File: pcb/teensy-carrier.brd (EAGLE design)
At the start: 63.2 x 41.9 mm, 13 parts

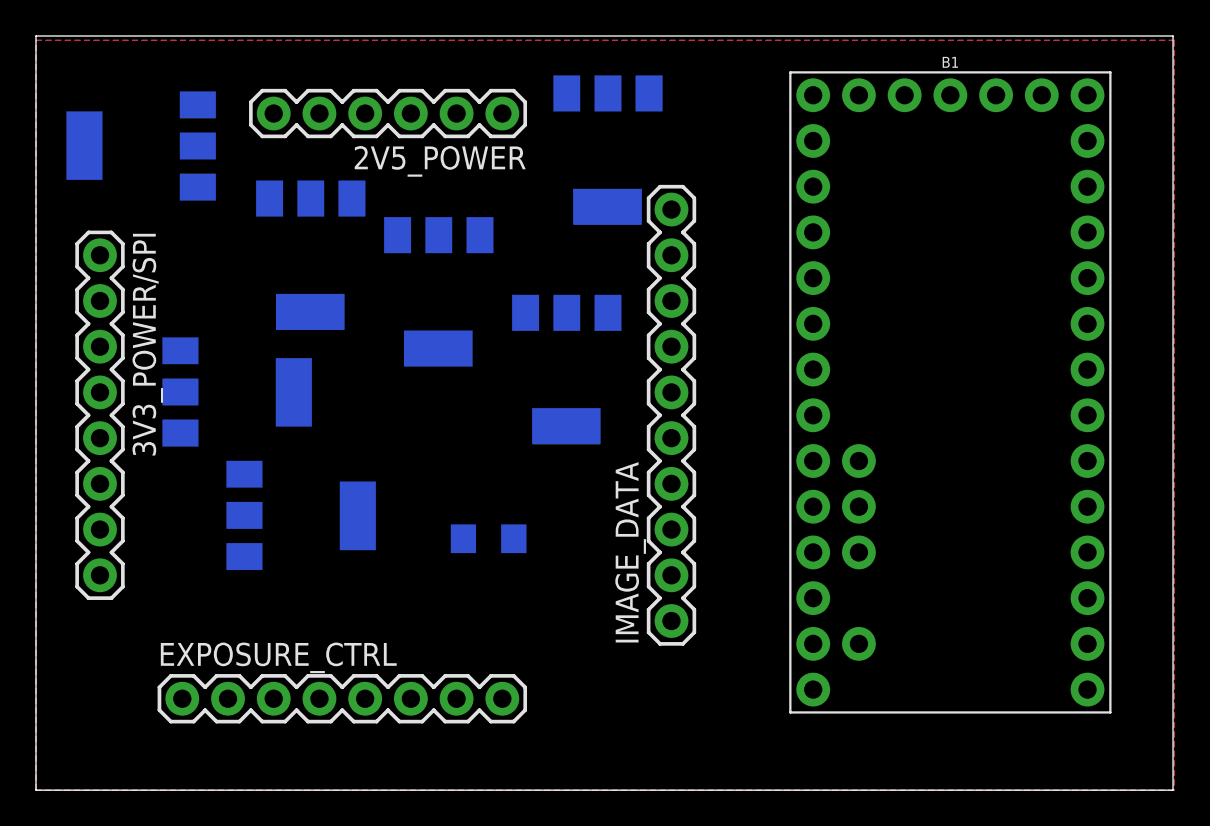
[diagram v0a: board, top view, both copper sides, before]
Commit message: finished teensy carrier and added image of dimensions
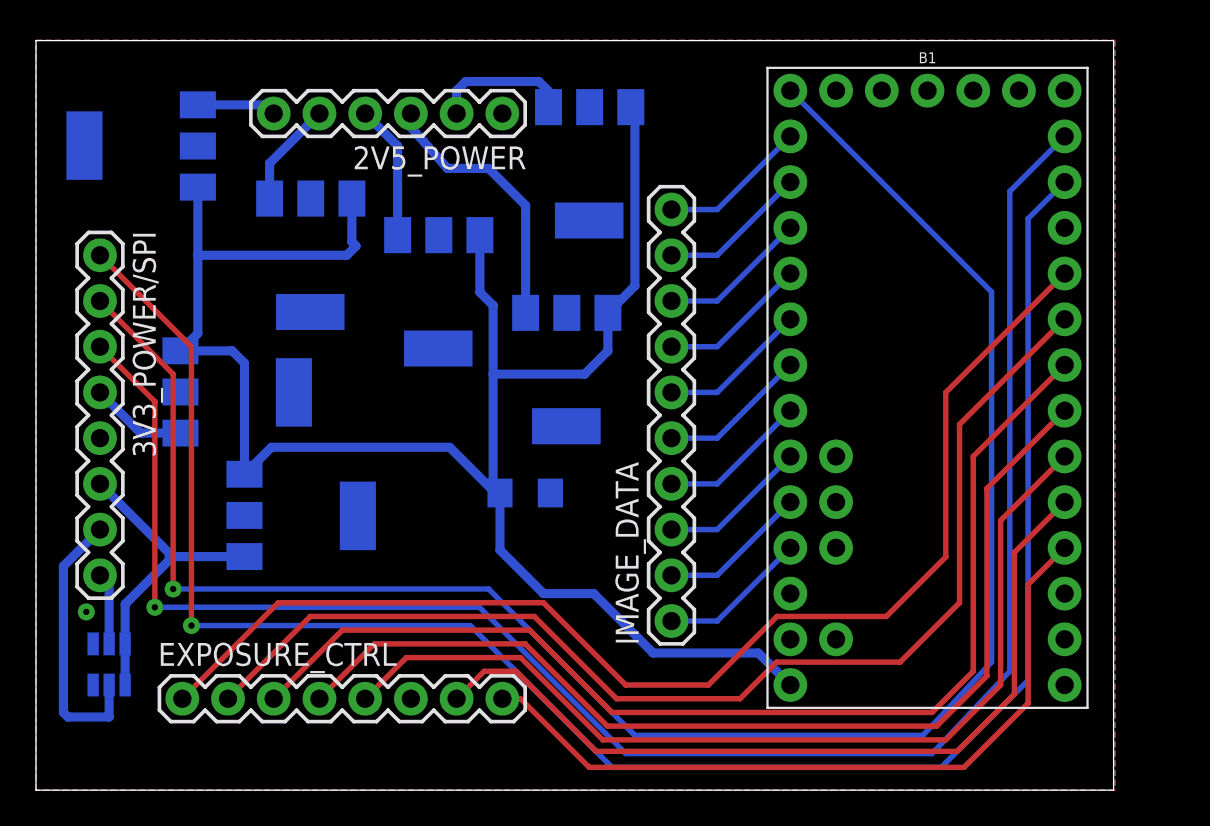
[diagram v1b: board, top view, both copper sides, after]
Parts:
- added SJ1, SJ3: (no value), SparkFun-Retired:SJ_3
- moved C1 3.25 mm to (27.2, 16.5)
- moved B1 1.30 mm to (49.5, 22.4)
- moved 2V5_10 1.27 mm to (30.7, 34.8)
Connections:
- net CLK: now also B1.2
- net FRAME_VALID: now also B1.7
- net GND: now also SJ1.3, SJ3.3
- net INT_TIME1: now also B1.4
- net INT_TIME2: now also B1.5
- net INT_TIME3: now also B1.6
- net LINE_VALID: now also B1.8
- net RESET: now also B1.3
- net VRESET_1: now also SJ1.1, SJ3.1
- net VRESET_2: now also SJ1.2
- net VRESET_3: now also SJ3.2
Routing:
- net VIN: track 0.00 -> 105.2 mm
- net SPI_CLK: track 0.00 -> 104.7 mm, vias 0 -> 1
- net SPI_EN: track 0.00 -> 102.9 mm, vias 0 -> 1
- net SPI_DATA: track 0.00 -> 99.6 mm, vias 0 -> 1
- net LINE_VALID: track 0.00 -> 68.0 mm
- net FRAME_VALID: track 0.00 -> 64.8 mm
- net INT_TIME3: track 0.00 -> 62.4 mm
- net INT_TIME2: track 0.00 -> 57.9 mm
- net INT_TIME1: track 0.00 -> 53.6 mm
- net RESET: track 0.00 -> 46.6 mm
- net CLK: track 0.00 -> 41.7 mm
- net VRESET_1: track 0.00 -> 18.1 mm
- net VRESET_2: track 0.00 -> 15.4 mm
- net VDDD: track 0.00 -> 15.0 mm
- net D2: track 0.00 -> 8.29 mm
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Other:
- board size 63.2 x 41.9 mm -> 59.9 x 41.6 mm
- board text added: "LUPA300 + Teensy3.2 Matt Ruffner 2017 v1.0"
